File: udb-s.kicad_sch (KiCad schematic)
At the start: 10 parts, among them J1 TYPE-C-31-M-12, J2 78171-0004, U1 TPD4E05U06DQAR

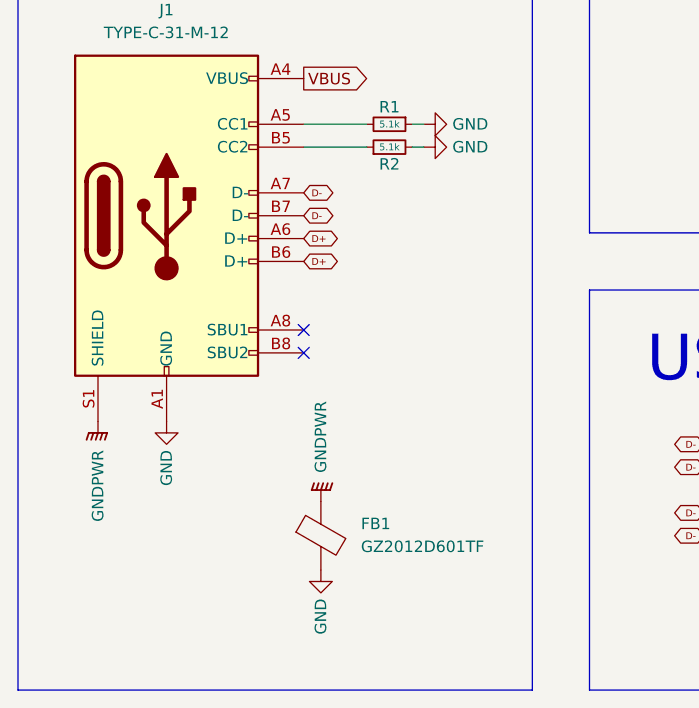
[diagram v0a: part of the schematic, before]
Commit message: Update grounding, remove FB1, new prod files
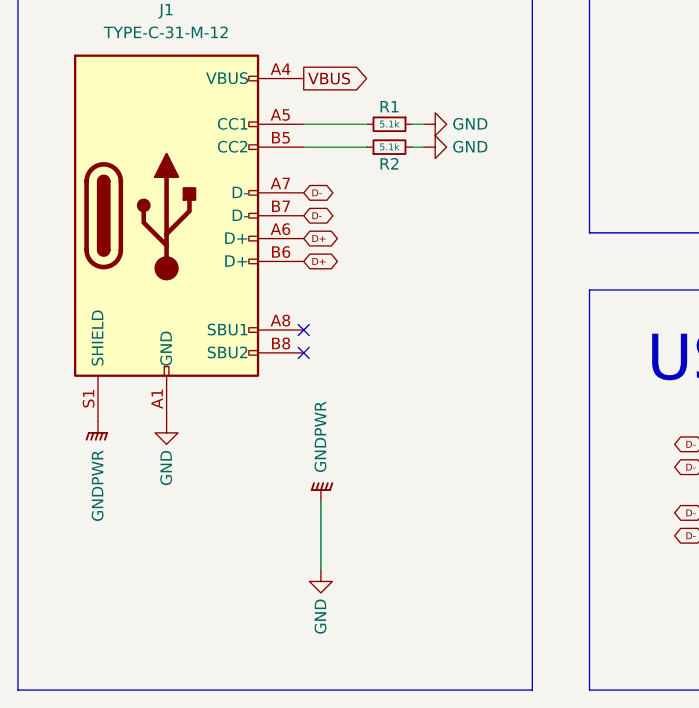
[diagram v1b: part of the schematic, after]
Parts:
- removed FB1: GZ2012D601TF, Inductor_SMD:L_0805_2012Metric, symbol Device:FerriteBead
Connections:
- net GNDPWR is gone; now on net GND: H1.1, J1.S1 (SHIELD)

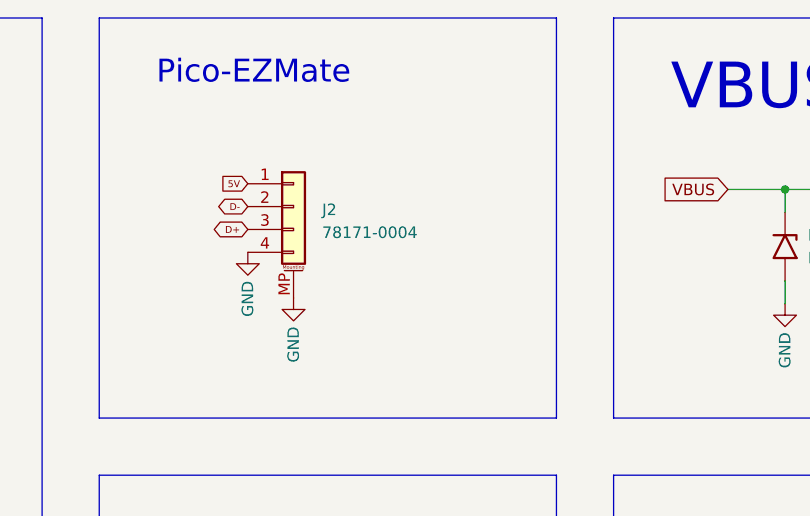
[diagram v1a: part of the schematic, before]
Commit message: Update submodules, change EZM for JST
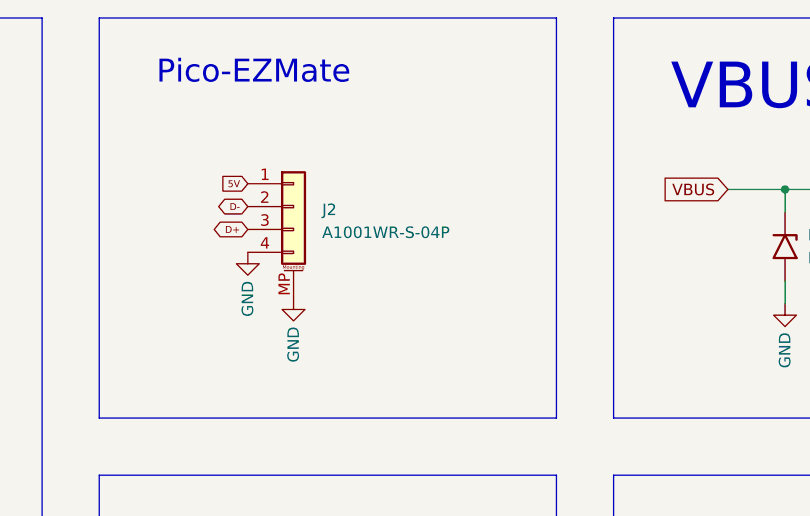
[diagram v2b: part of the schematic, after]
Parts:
- J2: value 78171-0004 -> A1001WR-S-04P; footprint locallib:PicoEZMate-Reinforced-Lite -> acheron_Connectors:SM04B-SRSS-TB(LF)(SN)_mounting-reliefs; LCSC Part Number C588524 -> C371510; Manufacturer MOLEX -> HR; Manufacturer Part Number 78171-0004 -> A1001WR-S-04P
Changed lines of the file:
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@@
 			)
 		)
-		(property "Value" "78171-0004"
+		(property "Value" "A1001WR-S-04P"
 			(at 177.165 49.2505 0)
 			(effects
@@
 			)
 		)
-		(property "Footprint" "locallib:PicoEZMate-Reinforced-Lite"
+		(property "Footprint" "acheron_Connectors:SM04B-SRSS-TB(LF)(SN)_mounting-reliefs"
 			(at 173.99 46.355 0)
 			(effects
@@
 			)
 		)
-		(property "Manufacturer" "MOLEX"
+		(property "Manufacturer" "HR"
 			(at 173.99 46.355 0)
 			(effects
@@
 			)
 		)
-		(property "Manufacturer Part Number" "78171-0004"
+		(property "Manufacturer Part Number" "A1001WR-S-04P"
 			(at 173.99 46.355 0)
 			(effects
@@
 			)
 		)
-		(property "LCSC Part Number" "C588524"
+		(property "LCSC Part Number" "C371510"
 			(at 173.99 46.355 0)
 			(effects
+				(font
+					(size 1.27 1.27)
+				)
+				(hide yes)
+			)
+		)
+		(property "Package" ""
+			(at 173.99 46.355 0)
+			(effects
